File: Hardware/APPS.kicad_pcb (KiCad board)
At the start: 2 copper layers, 100 x 75 mm, 81 parts, among them J4 Sygnały, J5 Diagnostyka, J8 Zasilanie+CAN, K1 FINDER-30.22, Q1 BSS138, SW1 SW_Push, U1 STM32L4P5RET6, U2 LM2596S-5, U3 LM1117-3.3, U4 LM1117-3.3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

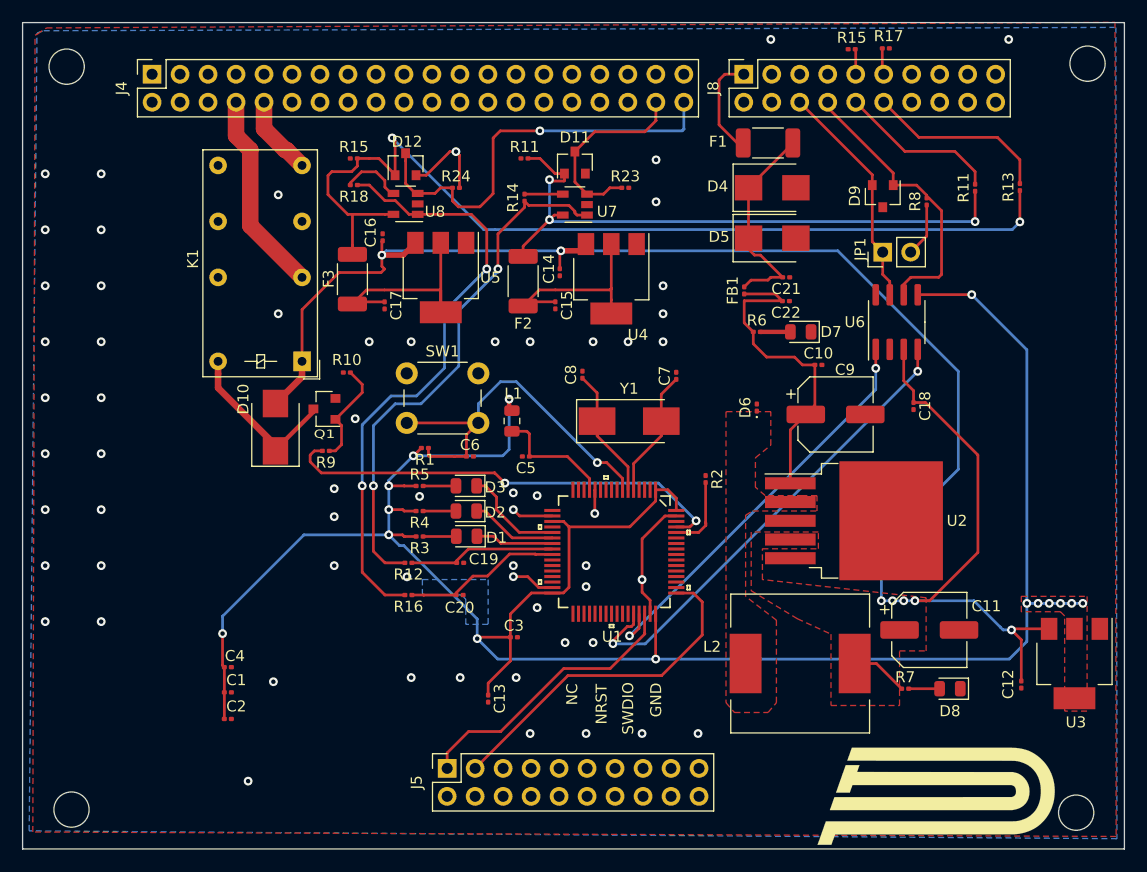
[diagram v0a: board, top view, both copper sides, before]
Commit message: PCB layout and routing
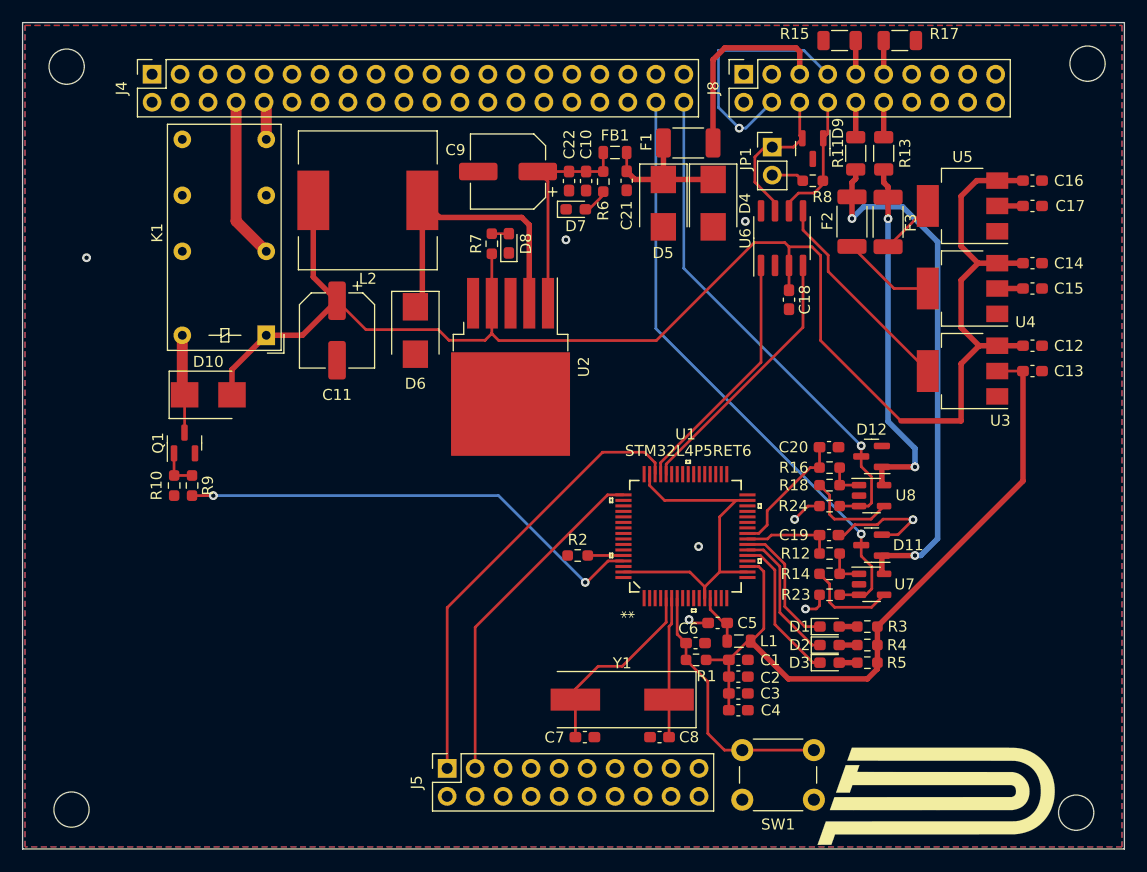
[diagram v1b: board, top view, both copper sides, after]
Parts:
- removed the R11 at (117.6, 64.9)
- removed the R11 at (158.5, 67.6)
- removed the R15 at (102.1, 64.9)
- removed the R15 at (147.3, 55.0)
- added R11: 220R, Resistor_SMD:R_1206_3216Metric, F.Cu at (147.7, 64.4)
- added R15: 0R, Resistor_SMD:R_1206_3216Metric, F.Cu at (146.2, 54.2)
- C1, C10, C12, C13, C14, C15, C16, C17, C18, C19, C2, C20, C21, C22, C3, C4, C5, C6, C7, C8: footprint Capacitor_SMD:C_0201_0603Metric -> Capacitor_SMD:C_0603_1608Metric_Pad1.08x0.95mm_HandSolder
- D1, D2, D3, D7, D8: footprint LED_SMD:LED_0805_2012Metric -> LED_SMD:LED_0603_1608Metric_Pad1.05x0.95mm_HandSolder
- D6: footprint Diode_SMD:D_0201_0603Metric -> Diode_SMD:D_SMB
- FB1: footprint Inductor_SMD:L_0201_0603Metric -> Inductor_SMD:L_0805_2012Metric
- R1, R10, R12, R14, R16, R18, R2, R23, R24, R3, R4, R5, R6, R7, R8, R9: footprint Resistor_SMD:R_0201_0603Metric -> Resistor_SMD:R_0603_1608Metric_Pad0.98x0.95mm_HandSolder
- R13, R17: footprint Resistor_SMD:R_0201_0603Metric -> Resistor_SMD:R_1206_3216Metric
- Y1: footprint Crystal:Crystal_SMD_0603-2Pin_6.0x3.5mm_HandSoldering -> Crystal:Crystal_SMD_HC49-SD
- moved C11 60.2 mm to (100.6, 80.5), turned to -90 degrees
- moved C17 59.5 mm to (163.7, 69.2), turned to 0 degrees
- moved C16 59.2 mm to (163.7, 66.9), turned to 0 degrees
- moved C13 57.7 mm to (163.7, 84.2), turned to 0 degrees
- moved L2 57.5 mm to (103.4, 68.7), turned to 180 degrees
- moved D8 56.9 mm to (116.2, 72.6), turned to 90 degrees
- moved R7 55.1 mm to (114.6, 72.6), turned to 90 degrees
- moved SW1 53.5 mm to (143.9, 123.1), turned to 180 degrees
- moved R18 51.1 mm to (145.3, 94.6)
- moved D12 49.9 mm to (149.1, 91.9), turned to 180 degrees
- moved U8 49.9 mm to (149.1, 95.5), turned to 0 degrees
- moved F3 48.9 mm to (150.6, 70.7)
- moved U5 47.8 mm to (157.4, 69.2), turned to 180 degrees
- moved C4 46.5 mm to (137.0, 115.0)
- moved C2 46.5 mm to (137.0, 111.9)
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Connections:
- J8 pad 1: +24V -> unconnected-(J8-Pad1)
- J8 pad 5: unconnected-(J8-Pad5) -> +24V
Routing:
- net /3V3_SYS: track 208.7 -> 85.0 mm, vias 15 -> 0
- net 3V3_POT2: track 86.8 -> 32.9 mm
- net Net-(R16-Pad2): track 55.3 -> 3.35 mm, vias 2 -> 0
- net Net-(R12-Pad2): track 48.4 -> 3.60 mm, vias 2 -> 0
- net GND: track 28.9 -> 72.3 mm, vias 61 -> 9
- net SIG_APPS1: track 17.9 -> 55.4 mm, vias 0 -> 1
- net Net-(D6-Pad1): track 0.00 -> 27.7 mm
- net /CAN-RX: track 43.6 -> 24.1 mm, vias 2 -> 0
- net +5V: track 165.6 -> 146.4 mm, vias 7 -> 0
- net SWD: track 25.7 -> 40.7 mm
- net /CAN-TX: track 37.7 -> 22.7 mm, vias 2 -> 0
- net CAN-L: track 26.0 -> 12.2 mm
- net Net-(J8-Pad12): track 16.7 -> 3.18 mm
- net Net-(C17-Pad1): track 19.9 -> 7.53 mm
- net Net-(J8-Pad10): track 14.6 -> 3.18 mm
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- removed copper zone on F.Cu, net +5V
- removed copper zone on B.Cu, net /3V3_SYS
- removed copper zone on F.Cu, net /3V3_SYS
- removed copper zone on F.Cu, net Net-(D6-Pad1)
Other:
- board text removed: "GND"
- board text removed: "NC"
- board text removed: "NRST"
- board text removed: "SWDIO"

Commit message: Deleted 24V section
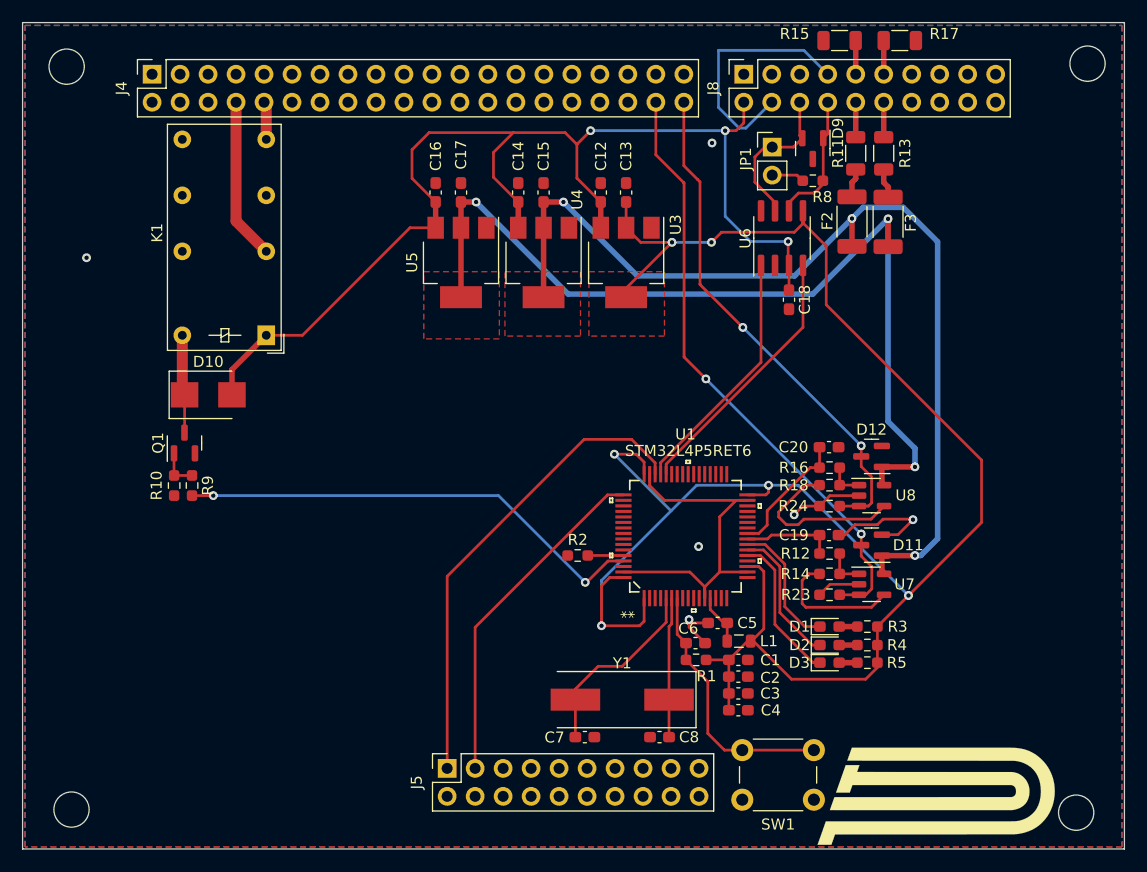
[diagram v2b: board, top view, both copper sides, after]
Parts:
- removed C10: 100nF, Capacitor_SMD:C_0603_1608Metric_Pad1.08x0.95mm_HandSolder
- removed C11: 220u, Capacitor_SMD:CP_Elec_6.3x7.7
- removed C21, C22: C_Small, Capacitor_SMD:C_0603_1608Metric_Pad1.08x0.95mm_HandSolder
- removed C9: 100u, Capacitor_SMD:CP_Elec_6.3x7.7
- removed D4: 30V, Diode_SMD:D_SMB
- removed D5: Fast diode, Diode_SMD:D_SMB
- removed D6: D_Schottky, Diode_SMD:D_SMB
- removed D7, D8: LED, LED_SMD:LED_0603_1608Metric_Pad1.05x0.95mm_HandSolder
- removed F1: 500mA, Fuse:Fuse_2010_5025Metric
- removed FB1: Ferrite_Bead_Small, Inductor_SMD:L_0805_2012Metric
- removed L2: 33u, Inductor_SMD:L_12x12mm_H8mm
- removed R6: 4k7R, Resistor_SMD:R_0603_1608Metric_Pad0.98x0.95mm_HandSolder
- removed R7: 680R, Resistor_SMD:R_0603_1608Metric_Pad0.98x0.95mm_HandSolder
- removed U2: LM2596S-5, Package_TO_SOT_SMD:TO-263-5_TabPin3
- R13: value 220R -> 0R
- R17: value 0R -> 220R
- moved C16 54.2 mm to (109.5, 68.0), turned to 90 degrees
- moved C17 51.9 mm to (111.8, 68.0), turned to 90 degrees
- moved C14 47.1 mm to (117.0, 68.0), turned to 90 degrees
- moved U5 45.8 mm to (111.8, 74.3), turned to -90 degrees
- moved C15 45.2 mm to (119.3, 68.0), turned to 90 degrees
- moved C12 41.6 mm to (124.5, 68.0), turned to 90 degrees
- moved C13 40.3 mm to (126.8, 68.0), turned to 90 degrees
- moved U4 38.1 mm to (119.3, 74.3), turned to -90 degrees
- moved U3 32.1 mm to (126.8, 74.3), turned to -90 degrees
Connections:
- C15 pad 1: Net-(C15-Pad1) -> 3V3_POT1
- C17 pad 1: Net-(C17-Pad1) -> 3V3_POT2
- F2 pad 2: Net-(C15-Pad1) -> 3V3_POT1
- F3 pad 2: Net-(C17-Pad1) -> 3V3_POT2
- J8 pad 2: unconnected-(J8-Pad2) -> +5V
- U4 pad 2: Net-(C15-Pad1) -> 3V3_POT1
- U5 pad 2: Net-(C17-Pad1) -> 3V3_POT2
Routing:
- net /3V3_SYS: track 85.0 -> 176.6 mm, vias 0 -> 6
- net 3V3_POT2: track 32.9 -> 87.2 mm, vias 2 -> 3
- net 3V3_POT1: track 48.5 -> 90.6 mm, vias 2 -> 3
- net +5V: track 146.4 -> 105.6 mm, vias 0 -> 3
- net +24V: track 31.2 -> 0.00 mm
- net Net-(D6-Pad1): track 27.7 -> 0.00 mm
- net Net-(C10-Pad1): track 20.0 -> 0.00 mm
- net Net-(C15-Pad1): track 10.8 -> 0.00 mm
- net GND: track 72.3 -> 80.6 mm, vias 9 -> 6
- net Net-(C17-Pad1): track 7.53 -> 0.00 mm
- net Net-(R18-Pad2): track 8.65 -> 15.7 mm
- net Net-(R14-Pad2): track 8.56 -> 12.0 mm
- net SWD: track 40.7 -> 43.4 mm
- net Net-(D7-Pad2): track 2.14 -> 0.00 mm
- net Net-(D8-Pad2): track 1.55 -> 0.00 mm
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- added copper zone on F.Cu, net /3V3_SYS
- added copper zone on F.Cu, net 3V3_POT1
- added copper zone on F.Cu, net 3V3_POT2

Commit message: Changed crystal footprint, fixed capactiors, added debug LED
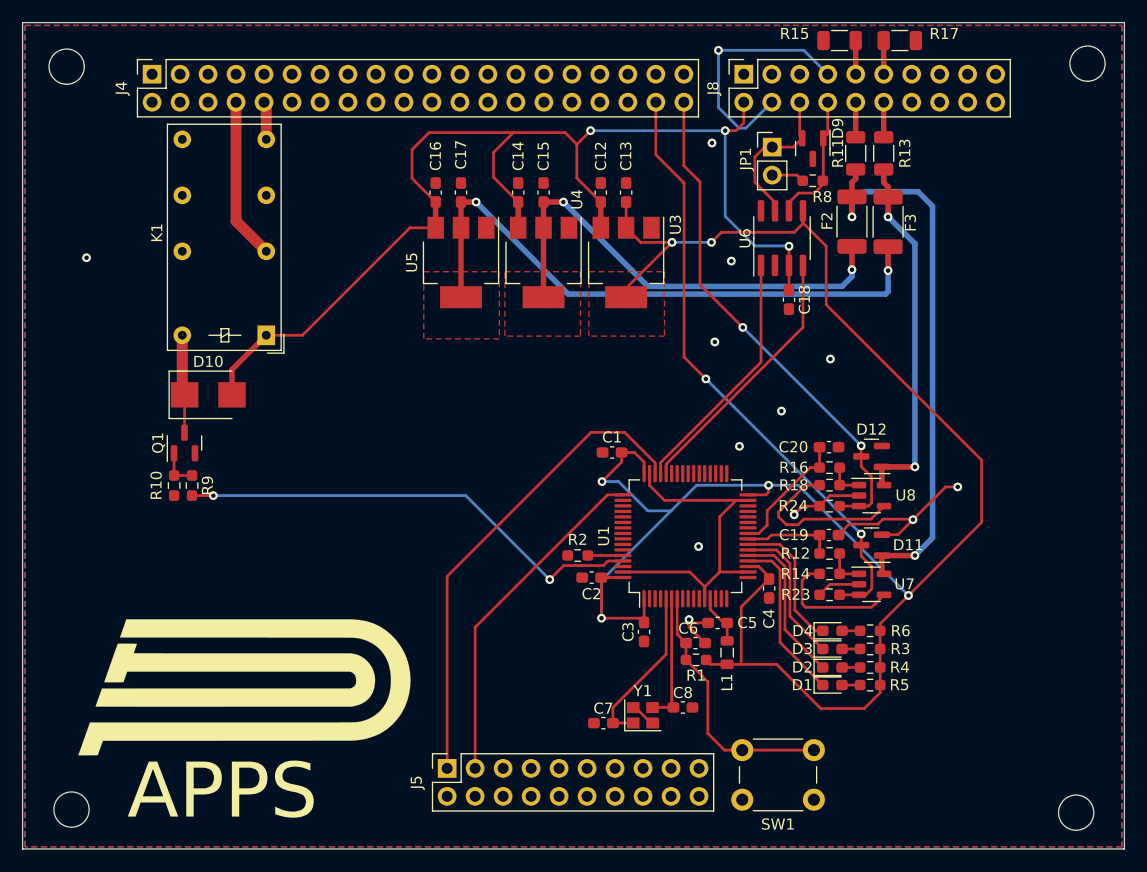
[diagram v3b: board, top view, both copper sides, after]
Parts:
- added D4: LED, LED_SMD:LED_0603_1608Metric_Pad1.05x0.95mm_HandSolder, F.Cu at (145.5, 107.8)
- added R6: 300R, Resistor_SMD:R_0603_1608Metric_Pad0.98x0.95mm_HandSolder, F.Cu at (149.0, 107.8)
- G***: footprint Logos:PUTM_LOGO_26mm -> Logos:PUTM_LOGO_35mm
- G***: footprint Logos:PUTM_LOGO_30mm -> Logos:PUTM_LOGO_35mm
- U1: footprint footprints:STM32L4P5RET6 -> Package_QFP:LQFP-64_10x10mm_P0.5mm
- Y1: value Crystal 8 MHz -> Crystal_GND24; footprint Crystal:Crystal_SMD_HC49-SD -> Crystal:Crystal_SMD_2520-4Pin_2.5x2.0mm
- moved G*** 63.8 mm to (91.3, 112.6)
- moved G*** 39.0 mm to (120.6, 85.1)
- moved C1 22.0 mm to (125.6, 91.6), turned to 180 degrees
- moved C2 16.1 mm to (123.7, 102.9), turned to 180 degrees
- moved C4 11.4 mm to (139.8, 103.9), turned to -90 degrees
- moved C3 10.2 mm to (128.4, 107.9), turned to -90 degrees
- moved G*** 9.13 mm to (92.8, 108.5)
- moved C8 3.43 mm to (132.0, 114.7), turned to 0 degrees
- moved Y1 2.36 mm to (128.3, 115.4), turned to 0 degrees
- moved C7 2.11 mm to (124.8, 116.2), turned to 180 degrees
- moved D1 2.05 mm to (145.5, 112.7)
- moved D2 2.05 mm to (145.5, 111.1)
- moved D3 2.05 mm to (145.5, 109.4)
- moved R3 2.05 mm to (149.0, 109.4)
- moved R4 2.05 mm to (149.0, 111.1)
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- renumbered D3 to D1, D1 to D3
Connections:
- C15 pad 1: 3V3_POT1 -> Net-(C15-Pad1)
- C17 pad 1: 3V3_POT2 -> Net-(C17-Pad1)
- F2 pad 2: 3V3_POT1 -> Net-(C15-Pad1)
- F3 pad 2: 3V3_POT2 -> Net-(C17-Pad1)
- U1 pad 20: unconnected-(U1-Pad20) -> /LED1
- U1 pad 21: /LED1 -> /LED2
- U1 pad 22: /LED2 -> /LED3
- U1 pad 23: /LED3 -> /LED4
- U4 pad 2: 3V3_POT1 -> Net-(C15-Pad1)
- U5 pad 2: 3V3_POT2 -> Net-(C17-Pad1)
- Y1 pad 1: /XTAL2 -> /XTAL1
- Y1 pad 2: /XTAL1 -> GND
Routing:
- net Net-(C17-Pad1): track 0.00 -> 55.0 mm, vias 0 -> 2
- net 3V3_POT2: track 87.2 -> 32.9 mm, vias 3 -> 2
- net Net-(C15-Pad1): track 0.00 -> 42.9 mm, vias 0 -> 2
- net 3V3_POT1: track 90.6 -> 51.0 mm, vias 3 -> 2
- net /LED4: track 0.00 -> 12.7 mm
- net GND: track 80.6 -> 88.2 mm, vias 6 -> 13
- net /3V3_SYS: track 176.6 -> 179.2 mm
- net /XTAL1: track 17.3 -> 15.1 mm
- net /LED1: track 13.5 -> 15.3 mm
- net /LED2: track 12.6 -> 14.4 mm
- net Net-(D4-Pad2): track 0.00 -> 1.64 mm
- net /LED3: track 11.9 -> 13.3 mm
- net /XTAL2: track 12.7 -> 11.8 mm
- net SWD: track 43.4 -> 43.9 mm
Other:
- board text added: "APPS"
- board text added: "Patryk Gawron"

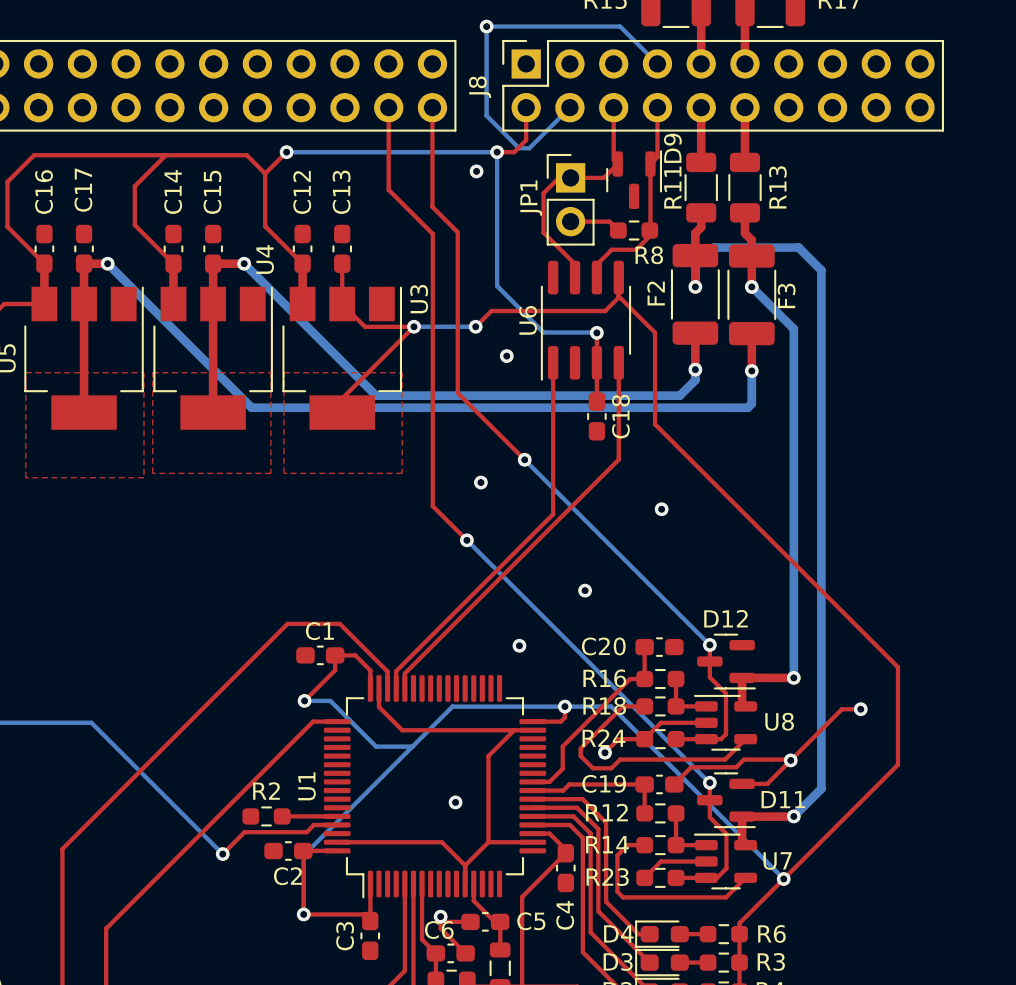
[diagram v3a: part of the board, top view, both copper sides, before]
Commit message: Fixed CAN lines to be equal length
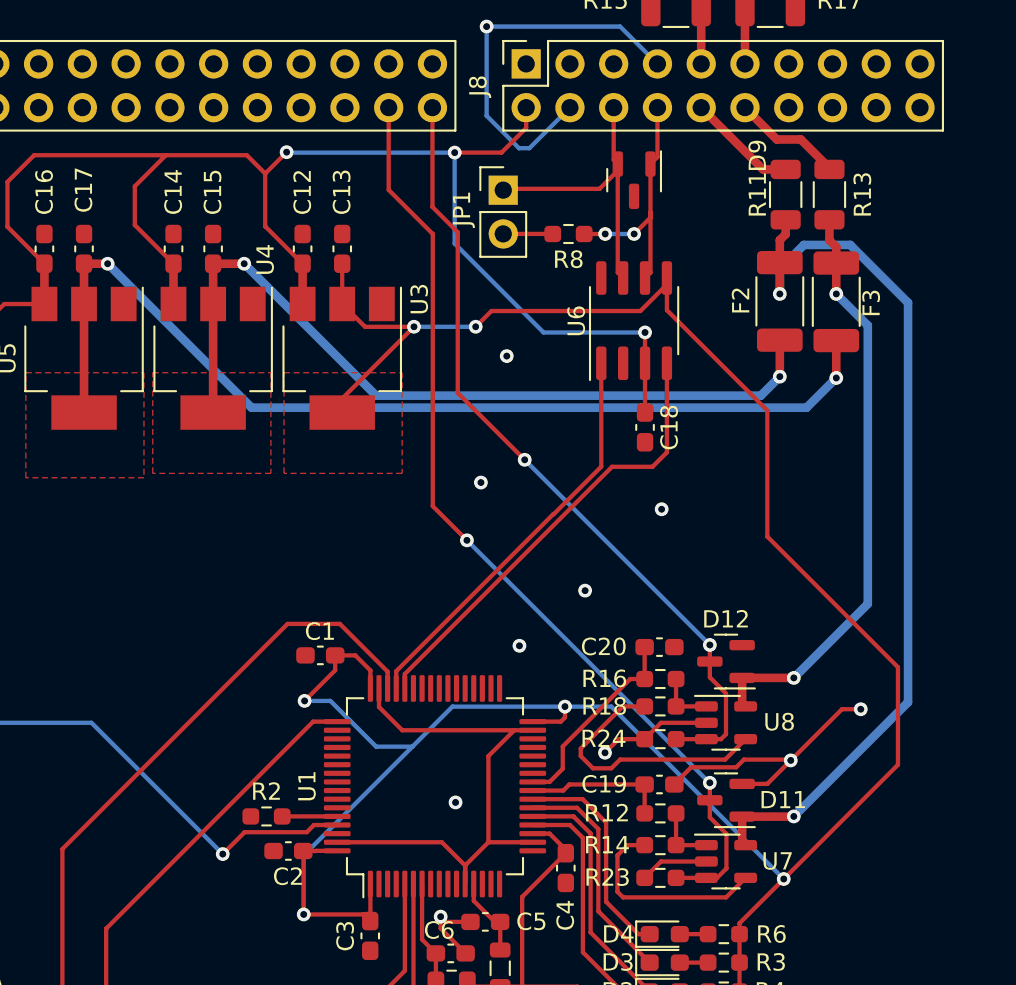
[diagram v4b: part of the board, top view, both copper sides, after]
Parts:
- moved R13 4.92 mm to (155.1, 64.8)
- moved F2 4.92 mm to (152.2, 71.0)
- moved F3 4.92 mm to (155.5, 71.1)
- moved R11 4.92 mm to (152.6, 64.8)
- moved JP1 3.98 mm to (136.2, 64.6)
- moved R8 3.82 mm to (140.0, 67.1)
- moved C18 2.87 mm to (144.4, 78.4)
- moved U6 2.79 mm to (143.8, 72.2)
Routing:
- net Net-(C15-Pad1): track 42.9 -> 47.3 mm
- net +5V: track 105.4 -> 109.5 mm
- net Net-(C17-Pad1): track 55.0 -> 58.6 mm
- net Net-(J8-Pad12): track 3.18 -> 6.43 mm
- net Net-(J8-Pad10): track 3.18 -> 6.39 mm
- net CAN-H: track 14.0 -> 17.0 mm
- net /CAN-RX: track 24.1 -> 26.6 mm
- net CAN-L: track 12.2 -> 14.6 mm, vias 0 -> 2
- net 3V3_POT1: track 51.0 -> 52.6 mm
- net /CAN-TX: track 22.7 -> 23.9 mm
- net /3V3_SYS: track 179.2 -> 180.3 mm
- net 3V3_POT2: track 32.9 -> 34.0 mm
- net GND: vias 13 -> 12

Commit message: Schematic cleanup
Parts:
- removed D11, D12: D_TVS_x2_AAC, Package_TO_SOT_SMD:SOT-23
- added D5: D_TVS, Diode_SMD:D_0603_1608Metric_Pad1.05x0.95mm_HandSolder, F.Cu at (150.4, 100.1)
- added D6: D_TVS, Diode_SMD:D_0603_1608Metric_Pad1.05x0.95mm_HandSolder, F.Cu at (150.4, 92.0)
- moved G*** 28.2 mm to (119.7, 99.9)
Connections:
- net Net-(C15-Pad1) renamed /PowerModule/VO_POT1
- net Net-(C17-Pad1) renamed /PowerModule/VO_POT2
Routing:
- net GND: track 88.2 -> 84.8 mm
- net SIG_APPS1: track 55.4 -> 57.2 mm
- net SIG_APPS2: track 46.4 -> 48.1 mm
- net 3V3_POT2: track 34.0 -> 32.8 mm
- net 3V3_POT1: track 52.6 -> 51.4 mm
- added copper zone on F.Cu, net /PowerModule/VO_POT1
- added copper zone on F.Cu, net /PowerModule/VO_POT2
- removed copper zone on F.Cu, net 3V3_POT1
- removed copper zone on F.Cu, net 3V3_POT2
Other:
- board text added: "SAFETY-IN"
- board text added: "SAFETY-OUT"
- board text removed: "- Supply +"
- board text removed: "CANH CANL"
- board text removed: "GND1 POT1 SUP1"
- board text removed: "GND2 POT2 SUP2"
- board text removed: "IN safety OUT"
